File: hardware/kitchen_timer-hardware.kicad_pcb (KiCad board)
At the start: 2 copper layers, 0 parts

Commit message: We started distributing componenets.
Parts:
- added C10: 10nF, Capacitor_SMD:C_0805_2012Metric_Pad1.18x1.45mm_HandSolder, F.Cu at (157.7, 102.9)
- added C11: 10nF, Capacitor_SMD:C_0805_2012Metric_Pad1.18x1.45mm_HandSolder, F.Cu at (154.7, 131.1)
- added C12: 10nF, Capacitor_SMD:C_0805_2012Metric_Pad1.18x1.45mm_HandSolder, F.Cu at (157.5, 131.1)
- added C13: 100nF, Capacitor_SMD:C_0805_2012Metric_Pad1.18x1.45mm_HandSolder, F.Cu at (156.2, 44.4)
- added C14: 100nF, Capacitor_SMD:C_0805_2012Metric_Pad1.18x1.45mm_HandSolder, F.Cu at (176.5, 44.4)
- added C15: 100nF, Capacitor_SMD:C_0805_2012Metric_Pad1.18x1.45mm_HandSolder, F.Cu at (156.2, 64.5)
- added C16: 100nF, Capacitor_SMD:C_0805_2012Metric_Pad1.18x1.45mm_HandSolder, F.Cu at (176.5, 64.5)
- added C5: 100nF, Capacitor_SMD:C_0805_2012Metric_Pad1.18x1.45mm_HandSolder, F.Cu at (142.7, 94.2)
- added C6: 100nF, Capacitor_SMD:C_0805_2012Metric_Pad1.18x1.45mm_HandSolder, F.Cu at (129.5, 92.2)
- added C7: 22pF, Capacitor_SMD:C_0805_2012Metric_Pad1.18x1.45mm_HandSolder, F.Cu at (145.8, 93.2)
- added C8: 22pF, Capacitor_SMD:C_0805_2012Metric_Pad1.18x1.45mm_HandSolder, F.Cu at (144.8, 86.9)
- added C9: 100nF, Capacitor_SMD:C_0805_2012Metric_Pad1.18x1.45mm_HandSolder, F.Cu at (137.7, 101.9)
- added D1: BAS40, Package_TO_SOT_SMD:SOT-23, F.Cu at (-66.8, 45.7)
- added D2: PMEG4010CEJ, Diode_SMD:D_SOD-323F, F.Cu at (-15.5, 0.80)
- added D3: Red test LED, LED_SMD:LED_0603_1608Metric_Pad1.05x0.95mm_HandSolder, F.Cu at (126.1, 96.8)
- added D4: Red test LED, LED_SMD:LED_0603_1608Metric_Pad1.05x0.95mm_HandSolder, F.Cu at (126.1, 99.9)
- added D5: Red test LED, LED_SMD:LED_0603_1608Metric_Pad1.05x0.95mm_HandSolder, F.Cu at (126.1, 103.1)
- added H1: MountingHole, MountingHole:MountingHole_2.2mm_M2, F.Cu at (-86.4, 14.6)
- added H2: MountingHole, MountingHole:MountingHole_2.2mm_M2, F.Cu at (-86.4, 20.5)
- added H3: MountingHole, MountingHole:MountingHole_2.2mm_M2, F.Cu at (-86.4, 26.5)
- added H4: MountingHole, MountingHole:MountingHole_2.2mm_M2, F.Cu at (-86.4, 32.4)
- added H5: MountingHole, MountingHole:MountingHole_2.2mm_M2, F.Cu at (-86.4, 38.4)
- added J1: Conn_01x02, kitchen_timer:JST_XH_1x02_P2.54mm_Vertical, B.Cu at (105.3, 127.7)
- added J2: Conn_01x02_Pin, Connector_PinHeader_2.54mm:PinHeader_1x02_P2.54mm_Vertical, F.Cu at (100.6, 115.1)
- added J3: AVR-ISP-6, Connector_PinHeader_2.54mm:PinHeader_2x03_P2.54mm_Vertical, F.Cu at (121.4, 79.0)
- added LS1: PS1240P02CT3, kitchen_timer:PS1240P02BT, F.Cu at (175.0, 88.3)
- added Q1: JSM2302, Package_TO_SOT_SMD:SOT-23, F.Cu at (-66.8, 50.4)
- added Q2: IRLML6402, Package_TO_SOT_SMD:SOT-23, F.Cu at (-20.1, 1.73)
- added Q3: MMBT3904, kitchen_timer:MMBT3904 (SOT-23), F.Cu at (-14.0, 19.9)
- added R1: 10k, Resistor_SMD:R_0805_2012Metric_Pad1.20x1.40mm_HandSolder, F.Cu at (-20.2, 5.42)
- added R10: 1k, Resistor_SMD:R_0805_2012Metric_Pad1.20x1.40mm_HandSolder, F.Cu at (121.9, 103.1)
- added R11: 10k, Resistor_SMD:R_0805_2012Metric_Pad1.20x1.40mm_HandSolder, F.Cu at (157.7, 105.2)
- added R12: 10k, Resistor_SMD:R_0805_2012Metric_Pad1.20x1.40mm_HandSolder, F.Cu at (148.9, 128.0)
- added R13: 10k, Resistor_SMD:R_0805_2012Metric_Pad1.20x1.40mm_HandSolder, F.Cu at (158.5, 128.0)
- added R14: 10k, Resistor_SMD:R_0805_2012Metric_Pad1.20x1.40mm_HandSolder, F.Cu at (153.7, 128.0)
- added R15: 10k, Resistor_SMD:R_0805_2012Metric_Pad1.20x1.40mm_HandSolder, F.Cu at (164.1, 128.0)
- added R16: 1k, Resistor_SMD:R_0805_2012Metric_Pad1.20x1.40mm_HandSolder, F.Cu at (-14.1, 13.1)
- added R17: 1k, Resistor_SMD:R_0805_2012Metric_Pad1.20x1.40mm_HandSolder, F.Cu at (-14.1, 16.0)
- added R18: 62K, Resistor_SMD:R_0805_2012Metric_Pad1.20x1.40mm_HandSolder, F.Cu at (156.2, 48.2)
- added R19: 62K, Resistor_SMD:R_0805_2012Metric_Pad1.20x1.40mm_HandSolder, F.Cu at (176.5, 48.2)
- added R20: 62K, Resistor_SMD:R_0805_2012Metric_Pad1.20x1.40mm_HandSolder, F.Cu at (156.2, 68.4)
- added R21: 62K, Resistor_SMD:R_0805_2012Metric_Pad1.20x1.40mm_HandSolder, F.Cu at (176.5, 68.3)
- added R6: 10k, Resistor_SMD:R_0805_2012Metric_Pad1.20x1.40mm_HandSolder, F.Cu at (136.7, 85.6)
- added R7: 1k, Resistor_SMD:R_0805_2012Metric_Pad1.20x1.40mm_HandSolder, F.Cu at (121.9, 96.8)
- added R8: 10k, Resistor_SMD:R_0805_2012Metric_Pad1.20x1.40mm_HandSolder, F.Cu at (137.7, 99.8)
- added R9: 1k, Resistor_SMD:R_0805_2012Metric_Pad1.20x1.40mm_HandSolder, F.Cu at (121.9, 99.9)
- added SW2: SKRPACE010, kitchen_timer:SW_SKRPACE010, F.Cu at (123.2, 90.2)
- added TP1: TestPoint, TestPoint:TestPoint_Pad_D2.0mm, F.Cu at (-81.4, 13.6)
- added TP10: TestPoint, TestPoint:TestPoint_Pad_D2.0mm, F.Cu at (-69.2, 13.6)
- added TP11: TestPoint, TestPoint:TestPoint_Pad_D2.0mm, F.Cu at (-69.2, 17.7)
- added TP12: TestPoint, TestPoint:TestPoint_Pad_D2.0mm, F.Cu at (-69.2, 21.7)
- added TP13: TestPoint, TestPoint:TestPoint_Pad_D2.0mm, F.Cu at (-65.2, 13.6)
- added TP14: TestPoint, TestPoint:TestPoint_Pad_D2.0mm, F.Cu at (-65.2, 17.7)
- added TP15: TestPoint, TestPoint:TestPoint_Pad_D2.0mm, F.Cu at (-65.2, 21.7)
- added TP16: TestPoint, TestPoint:TestPoint_Pad_D2.0mm, F.Cu at (-60.7, 13.7)
- added TP17: TestPoint, TestPoint:TestPoint_Pad_D2.0mm, F.Cu at (-60.7, 17.8)
- added TP2: TestPoint, TestPoint:TestPoint_Pad_D2.0mm, F.Cu at (-81.4, 17.7)
- added TP3: TestPoint, TestPoint:TestPoint_Pad_D2.0mm, F.Cu at (-81.4, 21.7)
- added TP4: TestPoint, TestPoint:TestPoint_Pad_D2.0mm, F.Cu at (-77.3, 13.6)
- added TP5: TestPoint, TestPoint:TestPoint_Pad_D2.0mm, F.Cu at (-77.3, 17.7)
- added TP6: TestPoint, TestPoint:TestPoint_Pad_D2.0mm, F.Cu at (-77.3, 21.7)
- added TP7: TestPoint, TestPoint:TestPoint_Pad_D2.0mm, F.Cu at (-73.3, 13.6)
- added TP8: TestPoint, TestPoint:TestPoint_Pad_D2.0mm, F.Cu at (-73.3, 17.7)
- added TP9: TestPoint, TestPoint:TestPoint_Pad_D2.0mm, F.Cu at (-73.3, 21.7)
- added U1: CH340E UART Module, kitchen_timer:CH340E_UART_BREAKOUT, B.Cu at (148.1, 154.0)
- added U10: MAX7219, Package_SO:SOIC-24W_7.5x15.4mm_P1.27mm, F.Cu at (166.4, 67.6)
- added U11: KWM-20882CUYB, kitchen_timer:KWM-20882CUYB, F.Cu at (146.1, 47.2)
- added U12: KWM-20882CUYB, kitchen_timer:KWM-20882CUYB, F.Cu at (166.4, 47.2)
- added U13: KWM-20882CUYB, kitchen_timer:KWM-20882CUYB, F.Cu at (146.1, 67.5)
- added U14: KWM-20882CUYB, kitchen_timer:KWM-20882CUYB, F.Cu at (166.4, 67.5)
- added U2: TP4056 breakout, kitchen_timer:TP4056_BREAKOUT, B.Cu at (132.8, 138.7)
- added U3: SparkFun_LiPower, kitchen_timer:SparkFun_LiPower, B.Cu at (111.0, 111.6)
- added U5: ATMEGA328P-AU, Package_QFP:TQFP-32_7x7mm_P0.8mm, F.Cu at (136.1, 93.2)
- added U6: PEC11R-4215F-S0024, kitchen_timer:PEC11R4215FS0024, F.Cu at (153.8, 109.2)
- added U7: MAX7219, Package_SO:SOIC-24W_7.5x15.4mm_P1.27mm, F.Cu at (146.1, 47.4)
- added U8: MAX7219, Package_SO:SOIC-24W_7.5x15.4mm_P1.27mm, F.Cu at (166.4, 47.4)
- added U9: MAX7219, Package_SO:SOIC-24W_7.5x15.4mm_P1.27mm, F.Cu at (146.1, 67.6)
- added Y1: Crystal-32kHz, kitchen_timer:FL26T2-32.000, F.Cu at (143.8, 90.4)
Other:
- board outline added: 15.2 x 13 mm

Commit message: Move components in closer to each other
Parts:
- U2: moved to F.Cu
- moved D1 241.5 mm to (160.7, 126.9), turned to 90 degrees
- moved Q1 227.8 mm to (147.7, 127.0), turned to 90 degrees
- moved Q2 215.2 mm to (173.1, 96.5)
- moved R16 211.6 mm to (176.0, 106.0), turned to -90 degrees
- moved R1 210.1 mm to (171.0, 92.5)
- moved D2 207.9 mm to (169.0, 96.6), turned to 90 degrees
- moved Q3 204.9 mm to (172.1, 105.5)
- moved R17 180.8 mm to (154.5, 81.2), turned to 90 degrees
- moved U3 66.8 mm to (174.5, 132.5)
- moved J2 65.3 mm to (165.0, 125.7)
- moved J3 62.9 mm to (182.0, 95.6), turned to 180 degrees
- moved J1 44.8 mm to (137.5, 96.7)
- moved U2 35.7 mm to (168.5, 139.5), turned to 0 degrees
- moved LS1 25.8 mm to (172.5, 114.0)
- moved C5 20.7 mm to (163.0, 90.0)
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
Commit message: Joint review with Nicolas
Changes in placement of components:
- Rotated uC 90 degrees clockwise to make it easier to route programmer
  header
- Rotated screens 180 degrees to get close to uC's MOSI pin
- Moved in some mounting holes (temporary until we have fixed the size)
- Some other small changes in placement
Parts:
- moved H4 288.1 mm to (178.0, 147.0)
- moved H5 266.4 mm to (180.0, 35.0)
- moved H3 252.9 mm to (136.0, 147.0)
- moved H1 244.8 mm to (149.0, 82.0)
- moved H2 242.7 mm to (156.0, 34.0)
- moved TP1 186.7 mm to (88.8, 90.5)
- moved TP10 186.7 mm to (101.0, 90.5)
- moved TP11 186.7 mm to (101.0, 94.5)
- moved TP12 186.7 mm to (101.0, 98.6)
- moved TP13 186.7 mm to (105.0, 90.5)
- moved TP14 186.7 mm to (105.0, 94.5)
- moved TP15 186.7 mm to (105.0, 98.6)
- moved TP16 186.7 mm to (109.5, 90.6)
- moved TP17 186.7 mm to (109.5, 94.7)
- moved TP2 186.7 mm to (88.8, 94.5)
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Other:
- board size 15.2 x 13 mm -> 69.8 x 124.5 mm

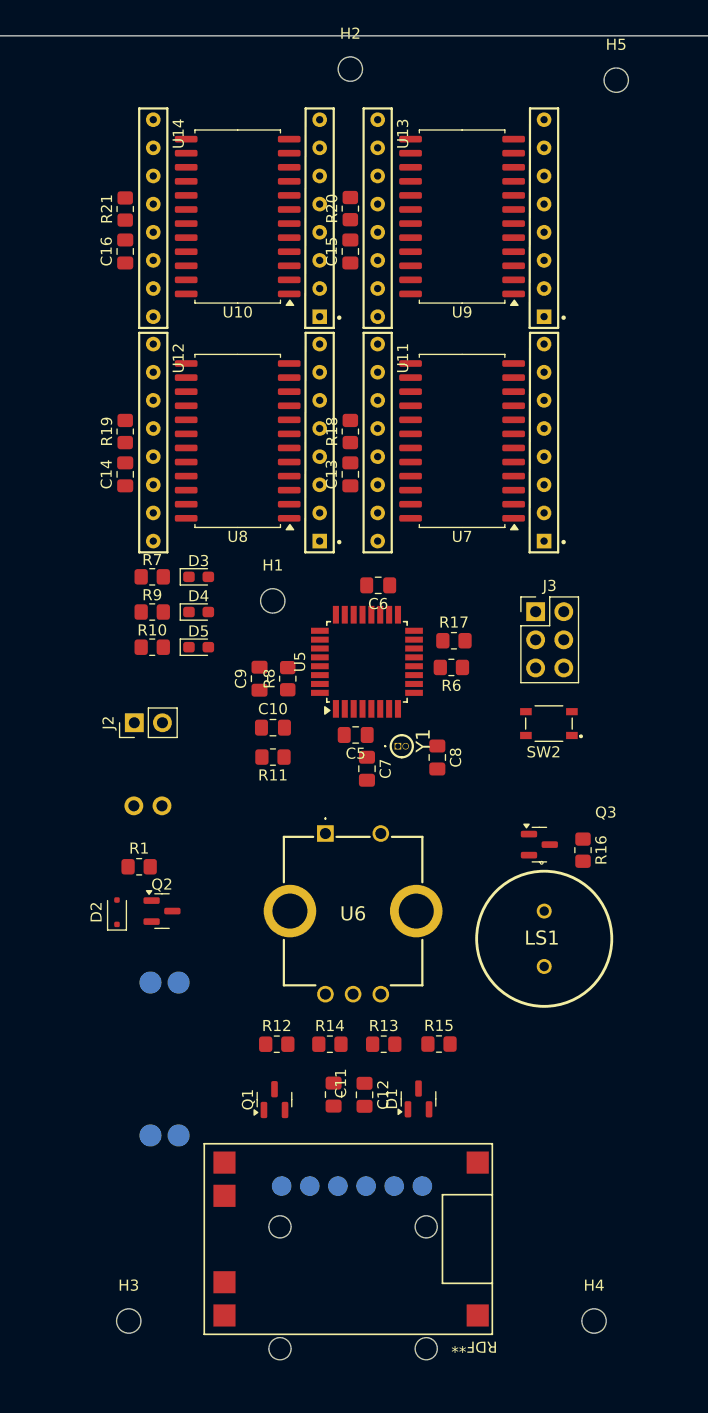
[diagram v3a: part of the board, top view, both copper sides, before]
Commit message: Changed the footprint of the crystal for one were the crystal is horizontal.
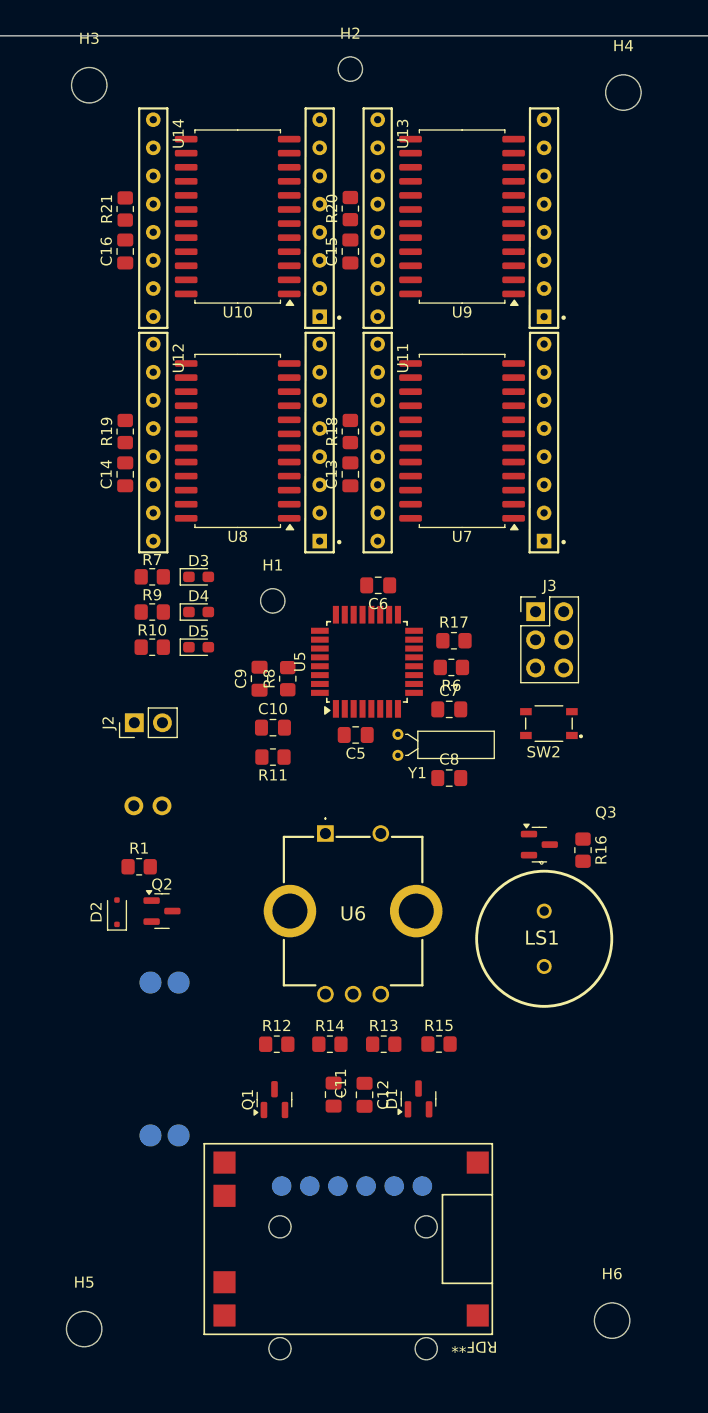
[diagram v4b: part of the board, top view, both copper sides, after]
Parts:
- added H6: MountingHole, MountingHole:MountingHole_3.2mm_M3, F.Cu at (179.6, 147.0)
- H3, H4, H5: footprint MountingHole:MountingHole_2.2mm_M2 -> MountingHole:MountingHole_3.2mm_M3
- Y1: footprint kitchen_timer:FL26T2-32.000 -> Crystal:Crystal_C26-LF_D2.1mm_L6.5mm_Horizontal
- moved H5 122.5 mm to (132.0, 147.7)
- moved H3 111.6 mm to (132.4, 35.5)
- moved H4 110.9 mm to (180.6, 36.1)
- moved C7 9.16 mm to (164.9, 91.8), turned to 0 degrees
- moved C8 2.15 mm to (164.9, 98.0), turned to 0 degrees
- moved Y1 0.83 mm to (160.3, 95.9), turned to 90 degrees

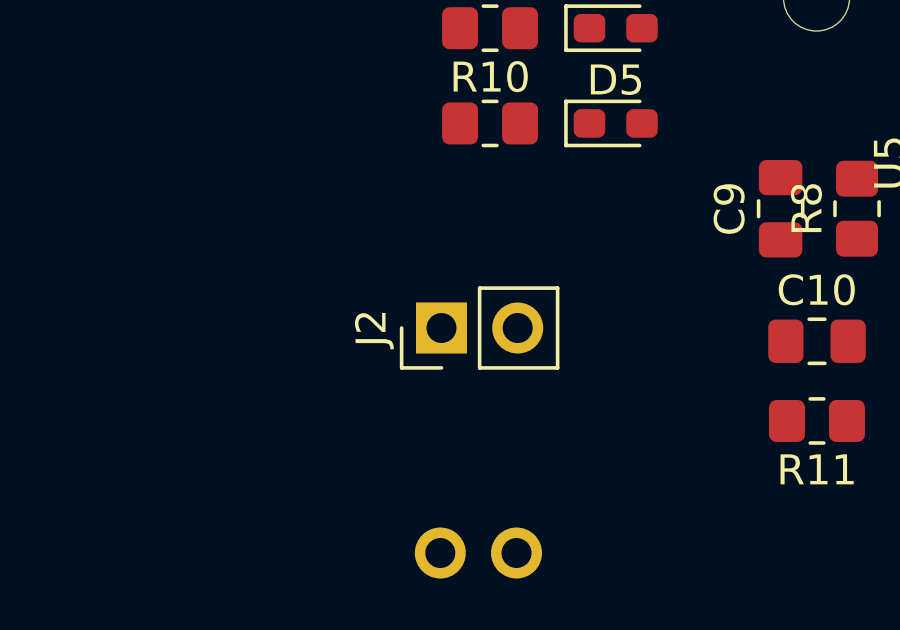
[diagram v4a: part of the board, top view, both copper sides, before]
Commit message: Changed the J2 connector for the same one as the J1
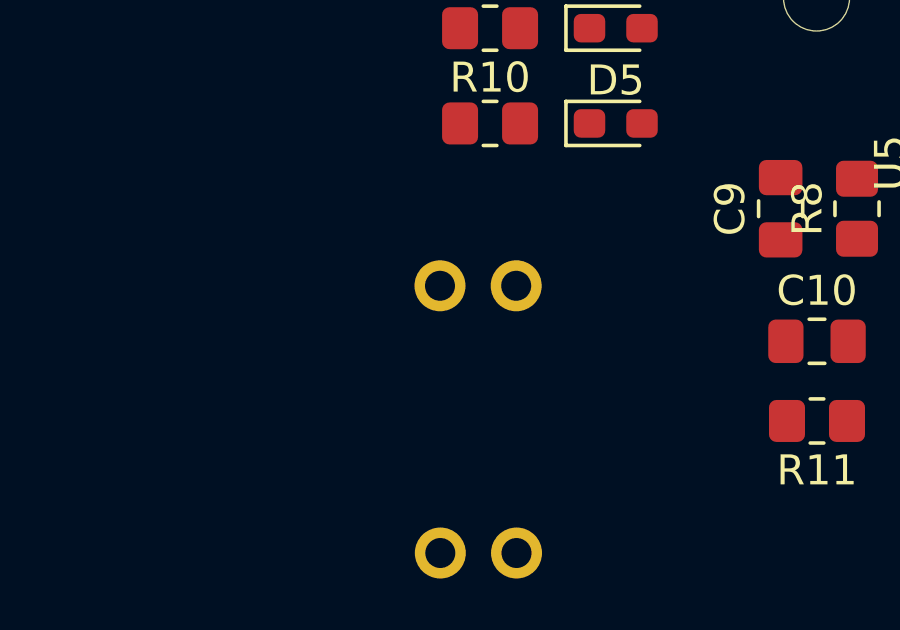
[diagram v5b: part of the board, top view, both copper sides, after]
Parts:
- J2: footprint Connector_PinHeader_2.54mm:PinHeader_1x02_P2.54mm_Vertical -> kitchen_timer:JST_XH_1x02_P2.54mm_Vertical; moved to B.Cu
- moved J2 4.46 mm to (134.0, 89.3), turned to 0 degrees
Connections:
- J2 pad 1: /+5V Boost Converter/PP_VCC_after_switch -> Net-(J2-Pin_1)
- J2 pad 2: Net-(J2-Pin_2) -> /+5V Boost Converter/PP_VCC_after_switch
